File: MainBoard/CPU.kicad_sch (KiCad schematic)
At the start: 23 parts, among them J3 prog, U1 W25Q128JVS, U2 RP2040, Y1 12MHz

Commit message: change schematic, use touch controller to enable second bard power. microcontroller should set pin up to latch power
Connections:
- net PWR_LATCH: now reaches U2.15 (GPIO12)
- net TOUCH_SYNC: no longer names the net of U2.13 (GPIO10)
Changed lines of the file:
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@@
+	)
+	(no_connect
+		(at 180.34 85.09)
 	)
 	(no_connect
@@
 		(at 180.34 118.11)
 	)
-	(no_connect
-		(at 180.34 90.17)
-	)
 	(wire
 		(pts
@@
 	(wire
 		(pts
-			(xy 180.34 85.09) (xy 182.88 85.09)
-		)
-		(stroke
-			(width 0)
-			(type default)
-		)
-	)
-	(wire
-		(pts
 			(xy 182.88 77.47) (xy 180.34 77.47)
 		)
@@
 		(pts
 			(xy 228.6 86.36) (xy 236.22 86.36)
+		)
+		(stroke
+			(width 0)
+			(type default)
+		)
+	)
+	(wire
+		(pts
+			(xy 180.34 90.17) (xy 182.88 90.17)
 		)
 		(stroke
@@
 		)
 	)
+	(hierarchical_label "PWR_LATCH"
+		(shape output)
+		(at 182.88 90.17 0)
+		(effects
+			(font
+				(size 1.27 1.27)
+			)
+			(justify left)
+		)
+	)
 	(hierarchical_label "ACCEL_INT2"
 		(shape bidirectional)
@@
 		)
 	)
-	(hierarchical_label "TOUCH_SYNC"
-		(shape input)
-		(at 182.88 85.09 0)
-		(effects
-			(font
-				(size 1.27 1.27)
-			)
-			(justify left)
-		)
-	)

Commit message: Change location of tuch sensor, touch button now power up all components, change length. Add buzzer to mainboard and remove touch from them. change revision version
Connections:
- net BUZZ: now reaches U2.16 (GPIO13)
- net SENS_PWR: no longer names the net of U2.12 (GPIO9)
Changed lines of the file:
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@@
-	)
-	(no_connect
-		(at 180.34 92.71)
 	)
 	(no_connect
@@
 	)
 	(no_connect
+		(at 180.34 82.55)
+	)
+	(no_connect
 		(at 180.34 123.19)
 	)
@@
 	(wire
 		(pts
-			(xy 180.34 82.55) (xy 182.88 82.55)
-		)
-		(stroke
-			(width 0)
-			(type default)
-		)
-	)
-	(wire
-		(pts
 			(xy 160.02 50.8) (xy 160.02 52.07)
 		)
@@
 		(pts
 			(xy 129.54 128.27) (xy 127 128.27)
+		)
+		(stroke
+			(width 0)
+			(type default)
+		)
+	)
+	(wire
+		(pts
+			(xy 180.34 92.71) (xy 182.88 92.71)
 		)
 		(stroke
@@
 		)
 	)
+	(hierarchical_label "BUZZ"
+		(shape output)
+		(at 182.88 92.71 0)
+		(effects
+			(font
+				(size 1.27 1.27)
+			)
+			(justify left)
+		)
+	)
 	(hierarchical_label "SPI_MOSI"
 		(shape output)
@@
 		(effects
 			(font
-				(size 1.27 1.27)
-			)
-			(justify left)
-		)
-	)
-	(hierarchical_label "SENS_PWR"
-		(shape input)
-		(at 182.88 82.55 0)
-		(effects
-			(font

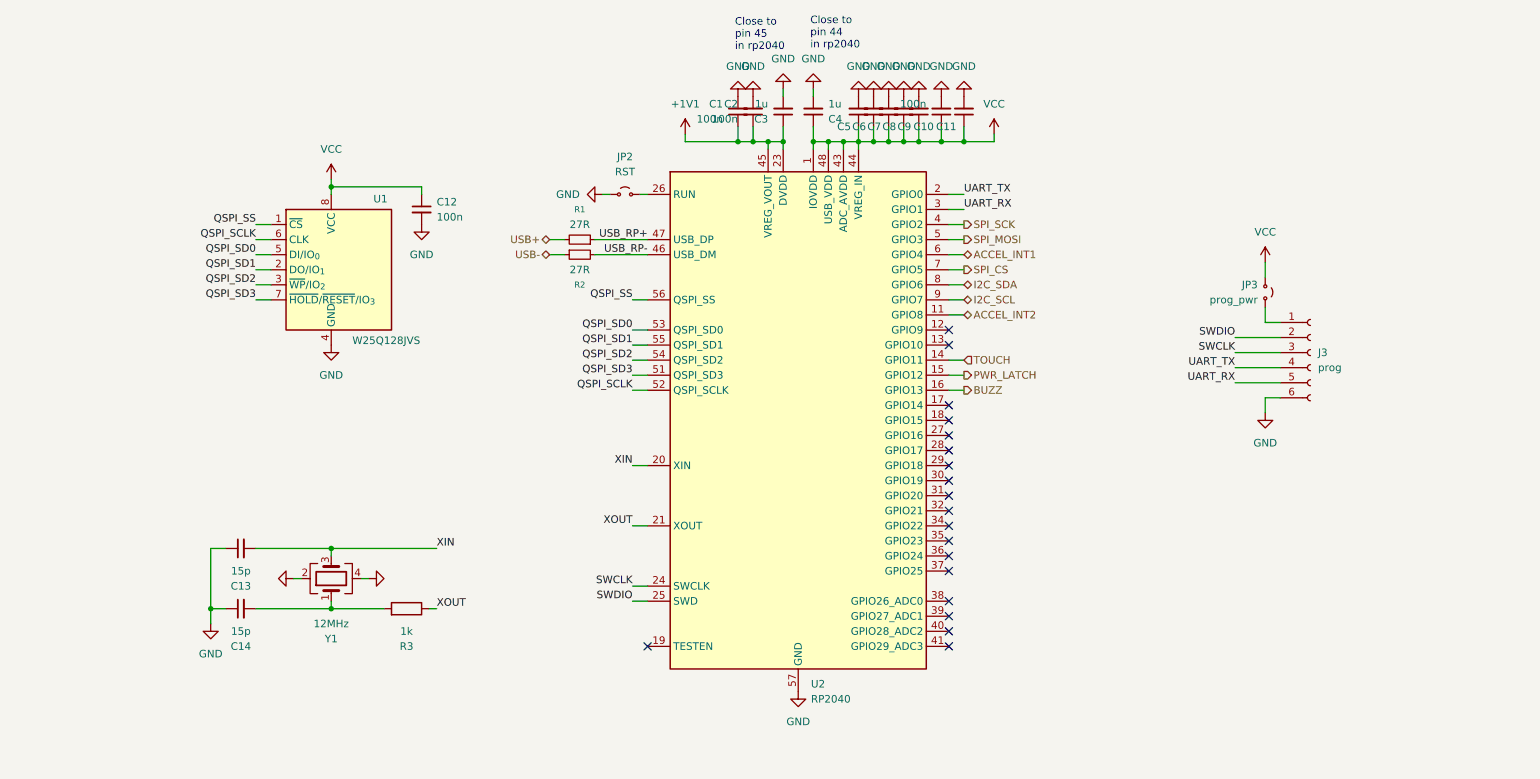
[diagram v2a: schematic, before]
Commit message: some changes for esp32 board
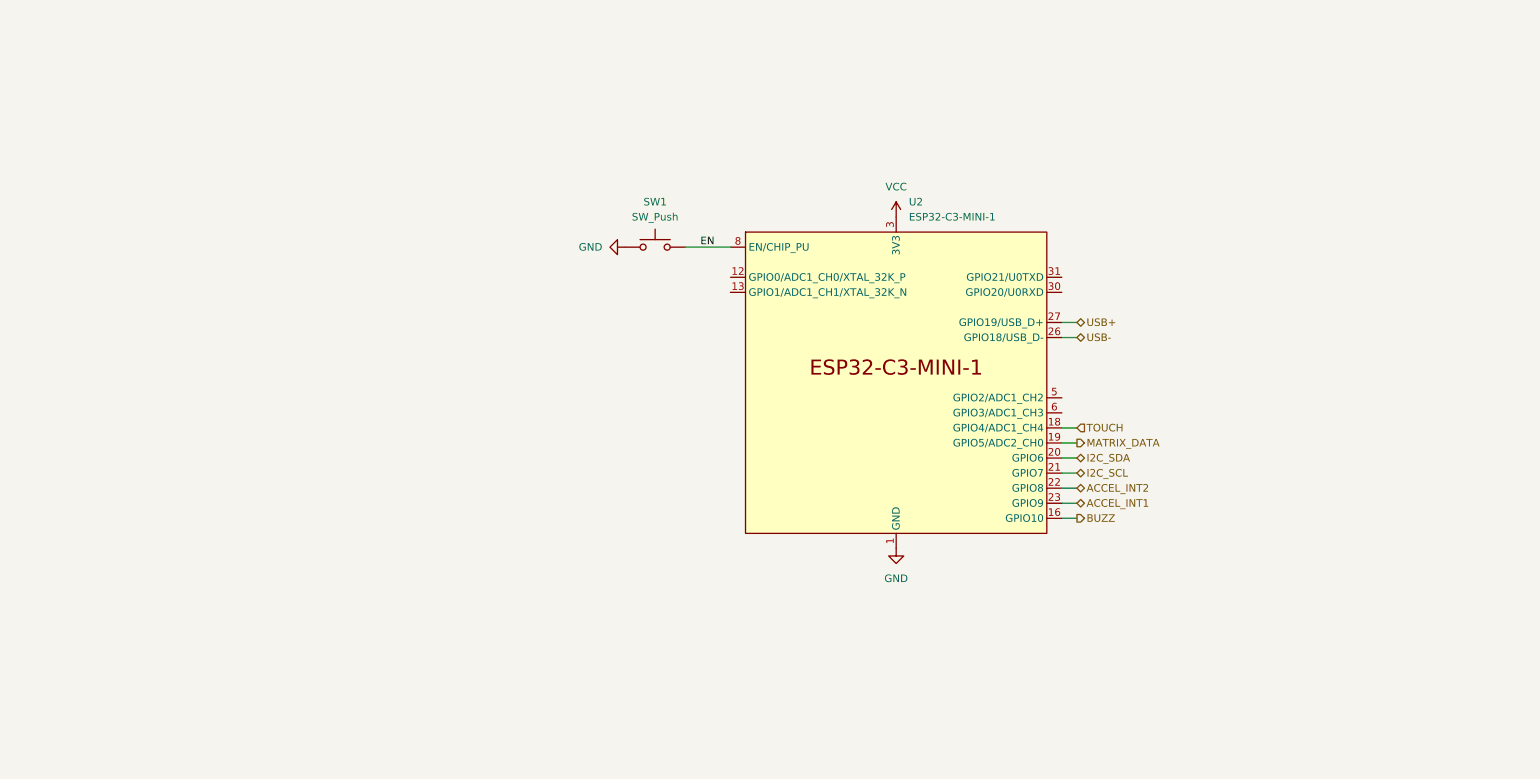
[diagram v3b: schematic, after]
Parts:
- removed C1, C10, C11, C12, C2, C5, C6, C7, C8, C9: 100n, Capacitor_SMD:C_0603_1608Metric_Pad1.08x0.95mm_HandSolder, symbol Device:C_Small
- removed C13, C14: 15p, Capacitor_SMD:C_0603_1608Metric_Pad1.08x0.95mm_HandSolder, symbol Device:C_Small
- removed C3, C4: 1u, Capacitor_SMD:C_0603_1608Metric_Pad1.08x0.95mm_HandSolder, symbol Device:C_Small
- removed J3: prog, Connector_JST:JST_SH_BM06B-SRSS-TB_1x06-1MP_P1.00mm_Vertical, symbol Connector:Conn_01x06_Socket
- removed JP2: RST, Jumper:SolderJumper-2_P1.3mm_Open_RoundedPad1.0x1.5mm, symbol Jumper:Jumper_2_Small_Open
- removed JP3: prog_pwr, Jumper:SolderJumper-2_P1.3mm_Open_RoundedPad1.0x1.5mm, symbol Jumper:Jumper_2_Small_Open
- removed R1, R2: 27R, Resistor_SMD:R_0603_1608Metric_Pad0.98x0.95mm_HandSolder, symbol Device:R_Small
- removed R3: 1k, Resistor_SMD:R_0603_1608Metric_Pad0.98x0.95mm_HandSolder, symbol Device:R
- removed U1: W25Q128JVS, Package_SO:SOIC-8_5.3x5.3mm_P1.27mm, symbol Memory_Flash:W25Q128JVS
- removed U2: RP2040, Package_DFN_QFN:QFN-56-1EP_7x7mm_P0.4mm_EP3.2x3.2mm, symbol MCU_RaspberryPi:RP2040
- removed Y1: 12MHz, Crystal:Crystal_SMD_2520-4Pin_2.5x2.0mm, symbol Device:Crystal_GND24
- added SW1: SW_Push, Button_Switch_SMD:SW_SPST_CK_RS282G05A3, symbol Switch:SW_Push
- added U2: ESP32-C3-MINI-1, PCM_Espressif:ESP32-C3-MINI-1, symbol Espressif:ESP32-C3-MINI-1
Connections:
- net ACCEL_INT1: now also U2.23 (GPIO9)
- net ACCEL_INT2: now also U2.22 (GPIO8)
- net BUZZ: now also U2.16 (GPIO10)
- net GND: now also SW1.1, U2.1 (GND), U2.11 (GND), U2.14 (GND), U2.2 (GND), U2.36 (GND), U2.37 (GND), U2.38 (GND), U2.39 (GND), U2.40 (GND), U2.41 (GND), U2.42 (GND), U2.43 (GND), U2.44 (GND), U2.45 (GND), U2.46 (GND), U2.47 (GND), U2.48 (GND), U2.49 (GND), U2.50 (GND), U2.51 (GND), U2.52 (GND), U2.53 (GND)
- net I2C_SCL: now also U2.21 (GPIO7)
- net I2C_SDA: now also U2.20 (GPIO6)
- net TOUCH: now also U2.18 (GPIO4/ADC1_CH4)
- net USB+: now also U2.27 (GPIO19/USB_D+)
- net USB-: now also U2.26 (GPIO18/USB_D-)
- net VCC: now also U2.3 (3V3)
- new net EN: SW1.2, U2.8 (EN/CHIP_PU)
- new net MATRIX_DATA: U2.19 (GPIO5/ADC2_CH0)
- no-connect marks 19 -> 0
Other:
- note removed: "Close to pin 44 in rp2040"
- note removed: "Close to pin 45 in rp2040"

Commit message: change schematic
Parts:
- removed U2: ESP32-C3-MINI-1, PCM_Espressif:ESP32-C3-MINI-1, symbol Espressif:ESP32-C3-MINI-1
- added U5: ESP32-C3-WROOM-02, PCM_Espressif:ESP32-C3-WROOM-02, symbol PCM_Espressif:ESP32-C3-WROOM-02
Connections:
- net ACCEL_INT1: now also U5.8 (GPIO9)
- net ACCEL_INT2: now also U5.7 (GPIO8)
- net BUZZ: now also U5.10 (GPIO10)
- net EN: now also U5.2 (EN/CHIP_PU)
- net GND: now also U5.19 (GND), U5.9 (GND)
- net I2C_SCL: now also U5.6 (GPIO7)
- net I2C_SDA: now also U5.5 (GPIO6)
- net MATRIX_DATA: now also U5.4 (GPIO5/ADC2_CH0)
- net TOUCH: now also U5.3 (GPIO4/ADC1_CH4)
- net USB+: now also U5.14 (GPIO19/USB_D+)
- net USB-: now also U5.13 (GPIO18/USB_D-)
- net VCC: now also U5.1 (3V3)
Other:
- moved on the sheet: SW1

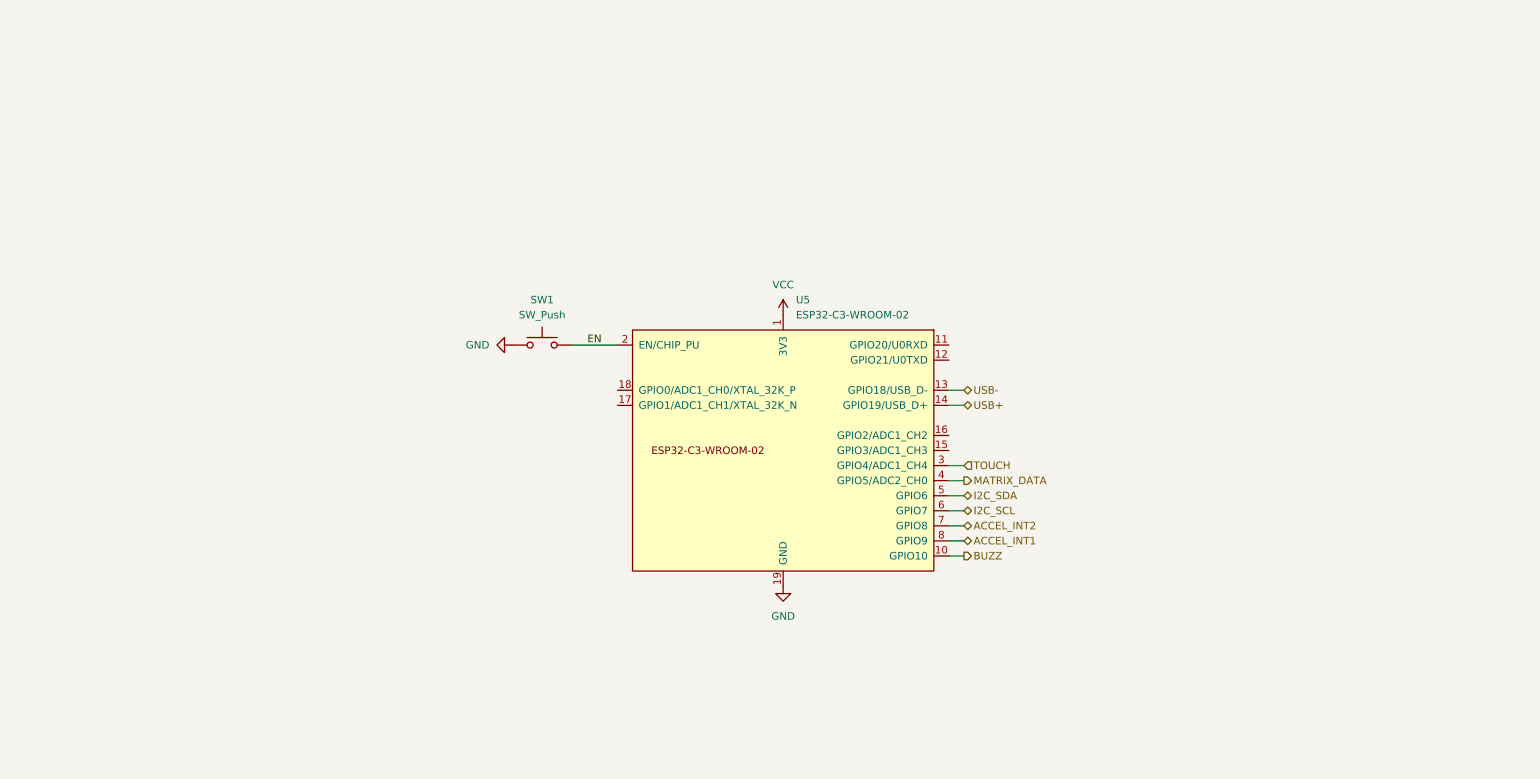
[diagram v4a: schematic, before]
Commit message: Change project assumptions, create new board with esp32-c3
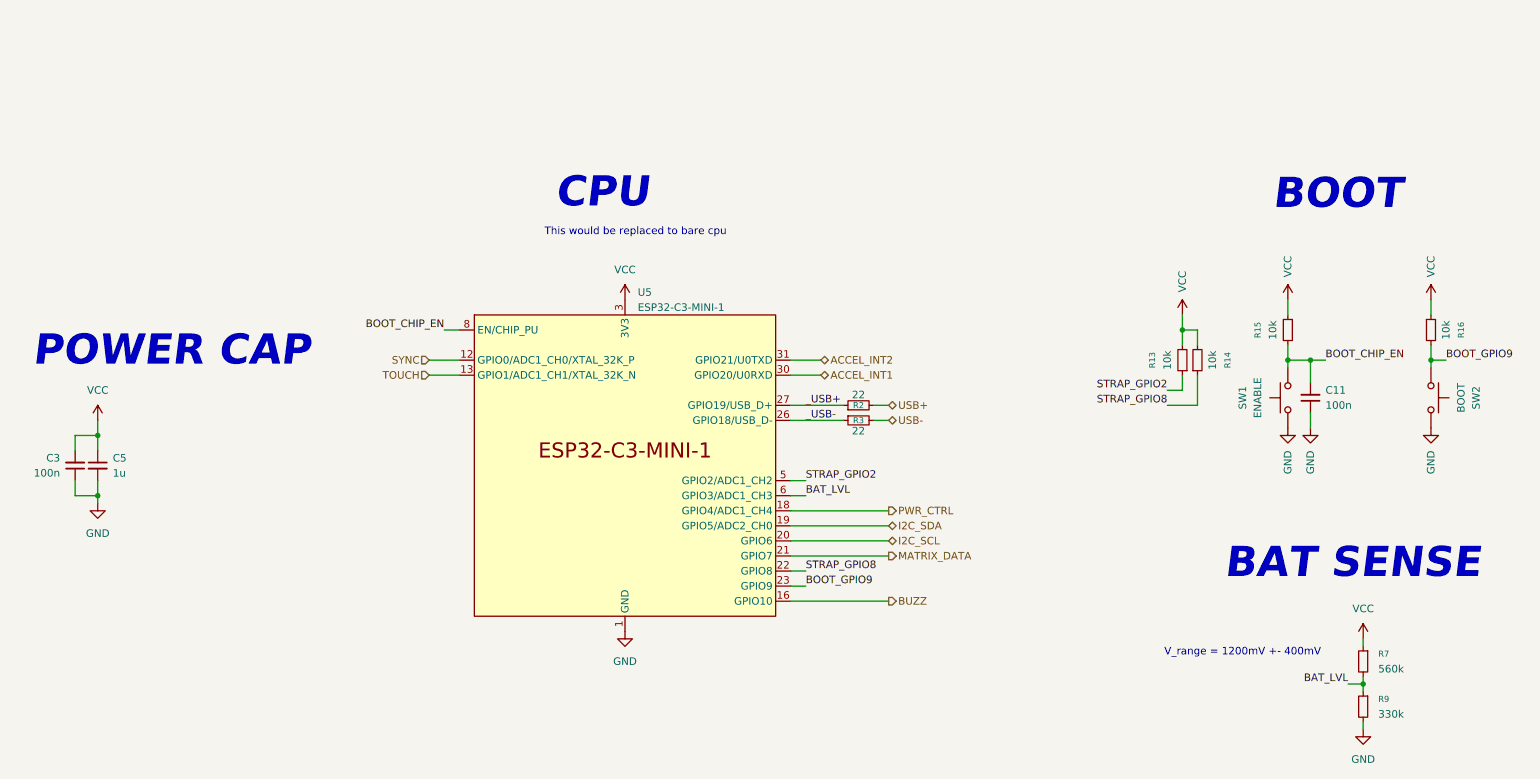
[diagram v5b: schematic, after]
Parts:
- removed U5: ESP32-C3-WROOM-02, PCM_Espressif:ESP32-C3-WROOM-02, symbol PCM_Espressif:ESP32-C3-WROOM-02
- added C11, C3: 100n, Capacitor_SMD:C_0603_1608Metric_Pad1.08x0.95mm_HandSolder, symbol Device:C_Small
- added C5: 1u, Capacitor_SMD:C_0603_1608Metric_Pad1.08x0.95mm_HandSolder, symbol Device:C_Small
- added R13, R14, R15, R16: 10k, Resistor_SMD:R_0603_1608Metric_Pad0.98x0.95mm_HandSolder, symbol Device:R_Small
- added R2, R3: 22, Resistor_SMD:R_0603_1608Metric_Pad0.98x0.95mm_HandSolder, symbol Device:R_Small
- added R7: 560k, Resistor_SMD:R_0603_1608Metric_Pad0.98x0.95mm_HandSolder, symbol Device:R_Small
- added R9: 330k, Resistor_SMD:R_0603_1608Metric_Pad0.98x0.95mm_HandSolder, symbol Device:R_Small
- added SW2: BOOT, Button_Switch_SMD:SW_SPST_CK_RS282G05A3, symbol Switch:SW_Push
- added U5: ESP32-C3-MINI-1, PCM_Espressif:ESP32-C3-MINI-1, symbol Espressif:ESP32-C3-MINI-1
- SW1: value SW_Push -> ENABLE
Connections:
- net ACCEL_INT1: now also U5.30 (GPIO20/U0RXD)
- net ACCEL_INT2: now also U5.31 (GPIO21/U0TXD)
- net BUZZ: now also U5.16 (GPIO10)
- net GND: now also C11.1, C3.1, C5.2, R9.2, SW2.1, U5.1 (GND), U5.11 (GND), U5.14 (GND), U5.2 (GND), U5.36 (GND), U5.37 (GND), U5.38 (GND), U5.39 (GND), U5.40 (GND), U5.41 (GND), U5.42 (GND), U5.43 (GND), U5.44 (GND), U5.45 (GND), U5.46 (GND), U5.47 (GND), U5.48 (GND), U5.49 (GND), U5.50 (GND), U5.51 (GND), U5.52 (GND), U5.53 (GND)
- net I2C_SCL: now also U5.20 (GPIO6)
- net I2C_SDA: now also U5.19 (GPIO5/ADC2_CH0)
- net MATRIX_DATA: now also U5.21 (GPIO7)
- net TOUCH: now also U5.13 (GPIO1/ADC1_CH1/XTAL_32K_N)
- net USB+: now also R2.2
- net USB-: now also R3.2
- net VCC: now also C3.2, C5.1, R13.2, R14.2, R15.1, R16.1, R7.1, U5.3 (3V3)
- net EN renamed BOOT_CHIP_EN
- net BOOT_CHIP_EN: now also C11.2, R15.2, U5.8 (EN/CHIP_PU)
- new net BAT_LVL: R7.2, R9.1, U5.6 (GPIO3/ADC1_CH3)
- new net BOOT_GPIO9: R16.2, SW2.2, U5.23 (GPIO9)
- new net PWR_CTRL: U5.18 (GPIO4/ADC1_CH4)
- new net STRAP_GPIO2: R13.1, U5.5 (GPIO2/ADC1_CH2)
- new net STRAP_GPIO8: R14.1, U5.22 (GPIO8)
- new net SYNC: U5.12 (GPIO0/ADC1_CH0/XTAL_32K_P)
- new net _USB+: R2.1, U5.27 (GPIO19/USB_D+)
- new net _USB-: R3.1, U5.26 (GPIO18/USB_D-)
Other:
- note added: "BAT SENSE"
- note added: "BOOT"
- note added: "CPU"
- note added: "POWER CAP"
- note added: "This would be replaced to bare cpu"
- note added: "V_range = 1200mV +- 400mV"
- moved on the sheet: SW1

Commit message: Udpate project variables and add texts
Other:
- title: blob -> VirtualBlob
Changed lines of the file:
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@@
 	(paper "A4")
 	(title_block
-		(title "blob")
+		(title "VirtualBlob")
 		(date "2025-09-15")
-		(rev "3")
+		(rev "0.4.0")
 		(company "Miłosz Derżko")
 	)

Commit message: Change naming of project
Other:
- company: Miłosz Derżko -> ${Company}
- title: VirtualBlob -> ${ProjectTitle}
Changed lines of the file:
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@@
 	(paper "A4")
 	(title_block
-		(title "VirtualBlob")
+		(title "${ProjectTitle}")
 		(date "2025-09-15")
-		(rev "0.4.0")
-		(company "Miłosz Derżko")
+		(rev "${Revision}")
+		(company "${Company}")
 	)
 	(text "CPU"
@@
 		)
 		(instances
-			(project "mainboard"
+			(project "MainBoard"
 				(path "/9e709b97-b403-4027-b7d8-a3ed3b3557e2/ebb18291-727f-4c7f-8948-aa188f83bb29"
 					(reference "#PWR019")
@@
 		)
 		(instances
-			(project "mainboard"
+			(project "MainBoard"
 				(path "/9e709b97-b403-4027-b7d8-a3ed3b3557e2/ebb18291-727f-4c7f-8948-aa188f83bb29"
 					(reference "#PWR045")
@@
 		)
 		(instances
-			(project "mainboard"
+			(project "MainBoard"
 				(path "/9e709b97-b403-4027-b7d8-a3ed3b3557e2/ebb18291-727f-4c7f-8948-aa188f83bb29"
 					(reference "C3")
@@
 		)
 		(instances
-			(project "mainboard"
+			(project "MainBoard"
 				(path "/9e709b97-b403-4027-b7d8-a3ed3b3557e2/ebb18291-727f-4c7f-8948-aa188f83bb29"
 					(reference "C5")
@@
 		)
 		(instances
-			(project "mainboard"
+			(project "MainBoard"
 				(path "/9e709b97-b403-4027-b7d8-a3ed3b3557e2/ebb18291-727f-4c7f-8948-aa188f83bb29"
 					(reference "R15")
@@
 		)
 		(instances
-			(project "mainboard"
+			(project "MainBoard"
 				(path "/9e709b97-b403-4027-b7d8-a3ed3b3557e2/ebb18291-727f-4c7f-8948-aa188f83bb29"
 					(reference "SW2")
@@
 		)
 		(instances
-			(project "mainboard"
+			(project "MainBoard"
 				(path "/9e709b97-b403-4027-b7d8-a3ed3b3557e2/ebb18291-727f-4c7f-8948-aa188f83bb29"
 					(reference "#PWR063")
@@
 		)
 		(instances
-			(project "mainboard"
+			(project "MainBoard"
 				(path "/9e709b97-b403-4027-b7d8-a3ed3b3557e2/ebb18291-727f-4c7f-8948-aa188f83bb29"
 					(reference "R2")
@@
 		)
 		(instances
-			(project "mainboard"
+			(project "MainBoard"
 				(path "/9e709b97-b403-4027-b7d8-a3ed3b3557e2/ebb18291-727f-4c7f-8948-aa188f83bb29"
 					(reference "R3")
@@
 		)
 		(instances
-			(project "mainboard"
+			(project "MainBoard"
 				(path "/9e709b97-b403-4027-b7d8-a3ed3b3557e2/ebb18291-727f-4c7f-8948-aa188f83bb29"
 					(reference "R13")
@@
 		)
 		(instances
-			(project "mainboard"
+			(project "MainBoard"
 				(path "/9e709b97-b403-4027-b7d8-a3ed3b3557e2/ebb18291-727f-4c7f-8948-aa188f83bb29"
 					(reference "#PWR049")
@@
 		)
 		(instances
-			(project "mainboard"
+			(project "MainBoard"
 				(path "/9e709b97-b403-4027-b7d8-a3ed3b3557e2/ebb18291-727f-4c7f-8948-aa188f83bb29"
 					(reference "R7")
@@
 		)
 		(instances
-			(project "mainboard"
+			(project "MainBoard"
 				(path "/9e709b97-b403-4027-b7d8-a3ed3b3557e2/ebb18291-727f-4c7f-8948-aa188f83bb29"
 					(reference "#PWR010")
@@
 		)
 		(instances
-			(project "mainboard"
+			(project "MainBoard"
 				(path "/9e709b97-b403-4027-b7d8-a3ed3b3557e2/ebb18291-727f-4c7f-8948-aa188f83bb29"
 					(reference "SW1")
@@
 		)
 		(instances
-			(project "mainboard"
+			(project "MainBoard"
 				(path "/9e709b97-b403-4027-b7d8-a3ed3b3557e2/ebb18291-727f-4c7f-8948-aa188f83bb29"
 					(reference "#PWR022")
@@
 		)
 		(instances
-			(project "mainboard"
+			(project "MainBoard"
 				(path "/9e709b97-b403-4027-b7d8-a3ed3b3557e2/ebb18291-727f-4c7f-8948-aa188f83bb29"
 					(reference "#PWR048")
@@
 		)
 		(instances
-			(project "mainboard"
+			(project "MainBoard"
 				(path "/9e709b97-b403-4027-b7d8-a3ed3b3557e2/ebb18291-727f-4c7f-8948-aa188f83bb29"
 					(reference "R14")
@@
 		)
 		(instances
-			(project "mainboard"
+			(project "MainBoard"
 				(path "/9e709b97-b403-4027-b7d8-a3ed3b3557e2/ebb18291-727f-4c7f-8948-aa188f83bb29"
 					(reference "#PWR09")
@@
 		)
 		(instances
-			(project "mainboard"
+			(project "MainBoard"
 				(path "/9e709b97-b403-4027-b7d8-a3ed3b3557e2/ebb18291-727f-4c7f-8948-aa188f83bb29"
 					(reference "R16")
@@
 		)
 		(instances
-			(project "mainboard"
+			(project "MainBoard"
 				(path "/9e709b97-b403-4027-b7d8-a3ed3b3557e2/ebb18291-727f-4c7f-8948-aa188f83bb29"
 					(reference "#PWR08")
@@
 		)
 		(instances
-			(project "mainboard"
+			(project "MainBoard"
 				(path "/9e709b97-b403-4027-b7d8-a3ed3b3557e2/ebb18291-727f-4c7f-8948-aa188f83bb29"
 					(reference "#PWR018")
@@
 		)
 		(instances
-			(project "mainboard"
+			(project "MainBoard"
 				(path "/9e709b97-b403-4027-b7d8-a3ed3b3557e2/ebb18291-727f-4c7f-8948-aa188f83bb29"
 					(reference "R9")
@@
 		)
 		(instances
-			(project "mainboard"
+			(project "MainBoard"
 				(path "/9e709b97-b403-4027-b7d8-a3ed3b3557e2/ebb18291-727f-4c7f-8948-aa188f83bb29"
 					(reference "C11")
@@
 		)
 		(instances
-			(project "mainboard"
+			(project "MainBoard"
 				(path "/9e709b97-b403-4027-b7d8-a3ed3b3557e2/ebb18291-727f-4c7f-8948-aa188f83bb29"
 					(reference "#PWR050")
@@
 		)
 		(instances
-			(project "mainboard"
+			(project "MainBoard"
 				(path "/9e709b97-b403-4027-b7d8-a3ed3b3557e2/ebb18291-727f-4c7f-8948-aa188f83bb29"
 					(reference "#PWR046")
